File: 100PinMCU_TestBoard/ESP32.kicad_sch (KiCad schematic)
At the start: 21 parts, among them J6 USB_C_Receptacle_USB2.0_16P, SW1 BOOT Switch, SW2 RESET Button, U1 ESP32-C6-MINI-1

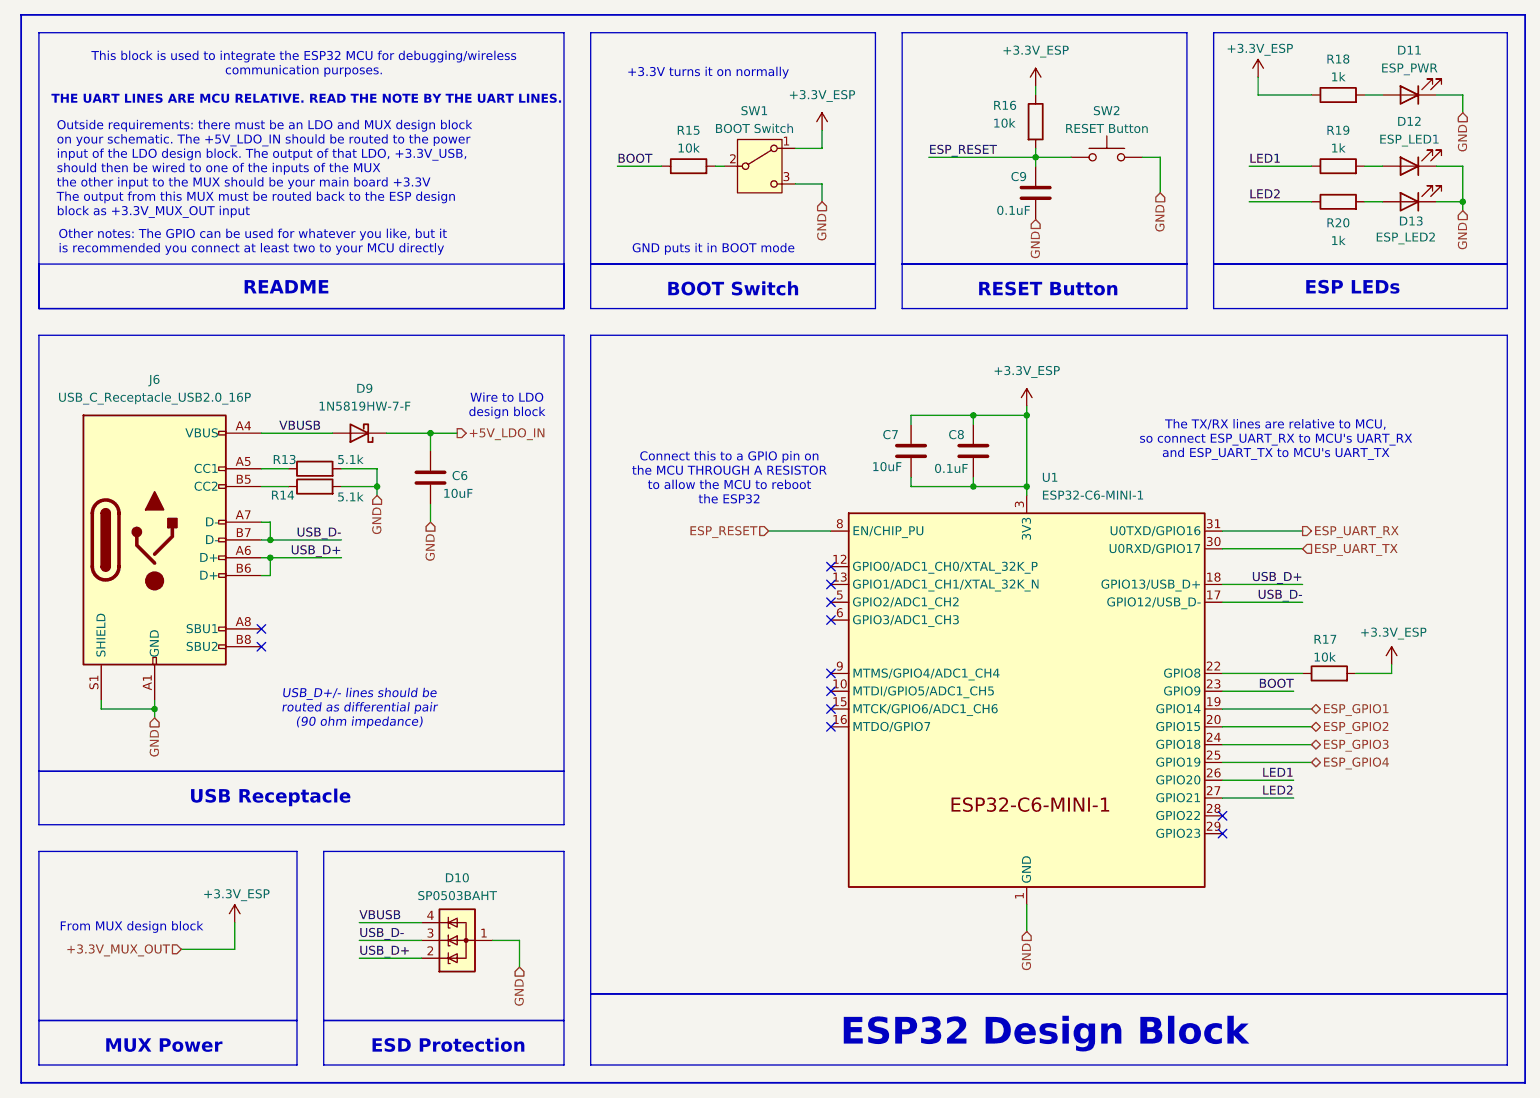
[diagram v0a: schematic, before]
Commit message: add mux
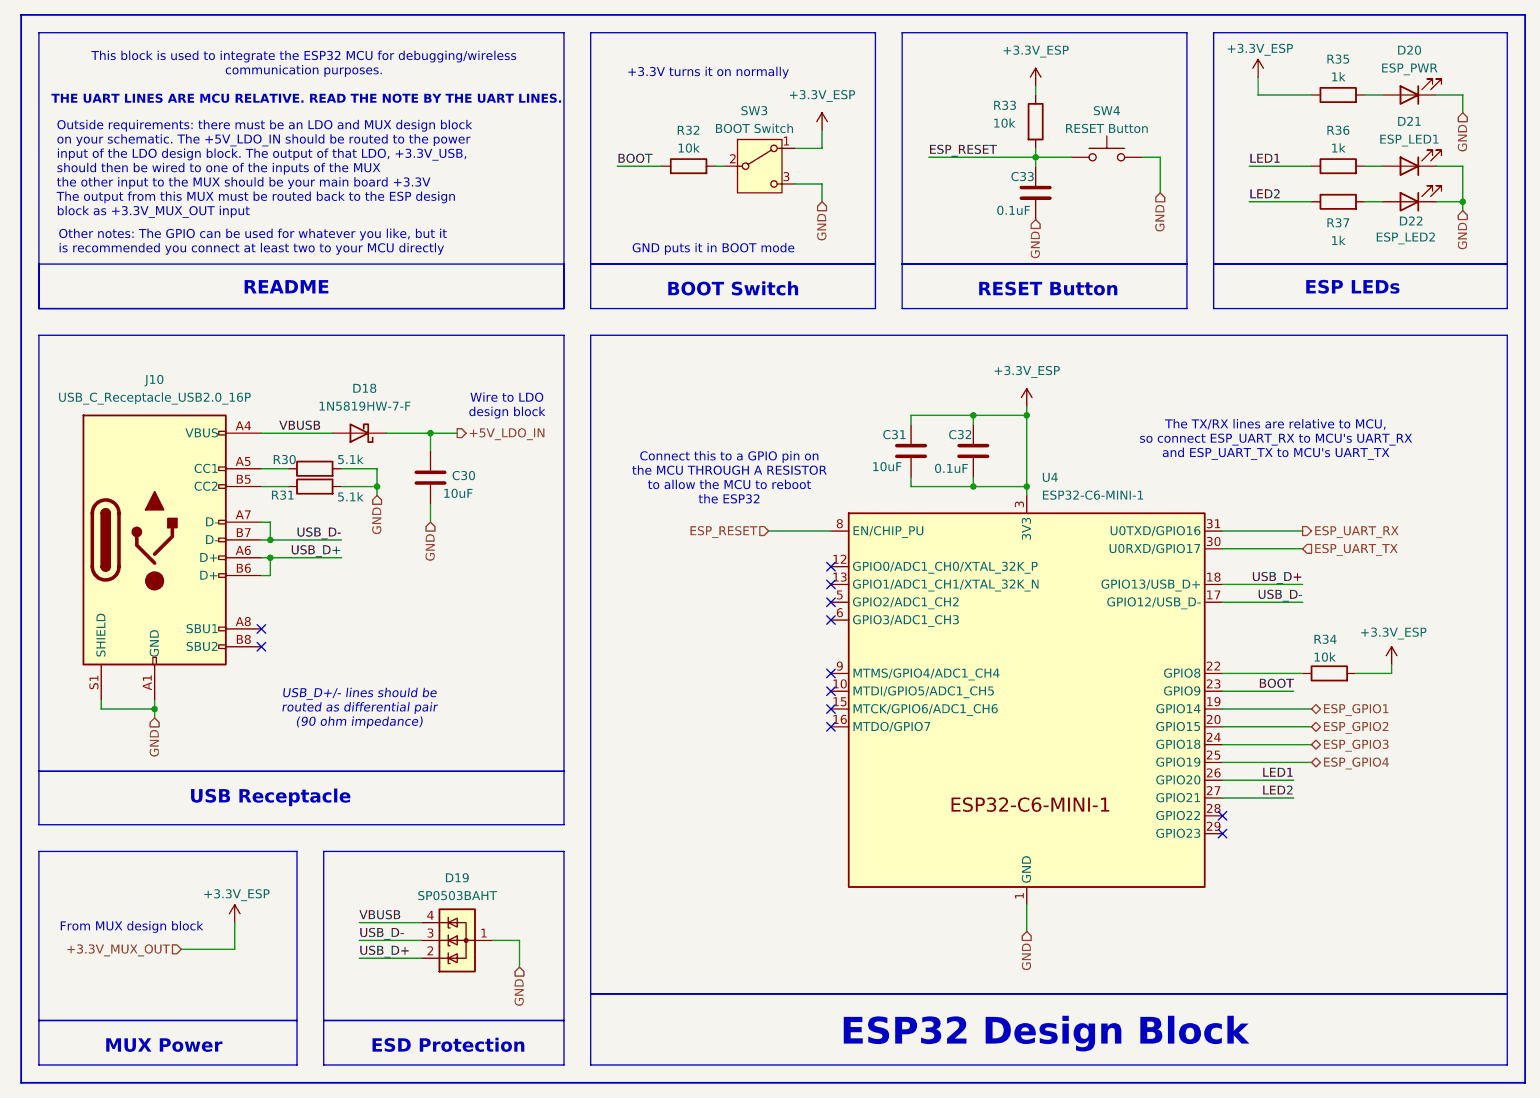
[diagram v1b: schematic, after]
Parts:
- renumbered C6 to C30, C7 to C31, C8 to C32, C9 to C33, D9 to D18, D10 to D19, D11 to D20, D12 to D21, D13 to D22, J6 to J10, R13 to R30, R14 to R31, R15 to R32, R16 to R33, R17 to R34, R18 to R35, R19 to R36, R20 to R37, SW1 to SW3, SW2 to SW4, U1 to U4
